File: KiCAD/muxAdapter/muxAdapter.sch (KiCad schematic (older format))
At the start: 55 parts, among them P1 CONN_01X01, P10 CONN_01X01, P11 CONN_01X01, P12 CONN_01X01, P13 CONN_01X01, P14 CONN_01X01, P15 CONN_01X01, P16 CONN_01X01, P17 CONN_01X01, P18 CONN_01X01, P19 CONN_01X01, P2 CONN_01X01, P20 CONN_01X01, P21 CONN_01X01, P22 CONN_01X01, P23 CONN_01X01, P24 CONN_01X01, P25 CONN_01X01, P26 CONN_01X01, P27 CONN_01X01, P28 CONN_01X01, P29 CONN_01X01, P3 CONN_01X01, P30 CONN_01X01, P31 CONN_01X01, P32 CONN_01X01, P33 CONN_01X01, P34 CONN_01X01, P35 CONN_01X01, P36 CONN_01X01, P37 CONN_01X01, P38 CONN_01X01, P39 CONN_01X02, P4 CONN_01X01, P40 CONN_01X02, P41 CONN_01X02, P42 CONN_01X02, P43 CONN_01X02, P44 CONN_01X02, P45 CONN_01X02, P46 CONN_01X02, P5 CONN_01X01, P6 CONN_01X01, P7 CONN_01X01, P8 CONN_01X01, P9 CONN_01X01, U1 MAX14662, U2 MAX14662, U3 PCF8574

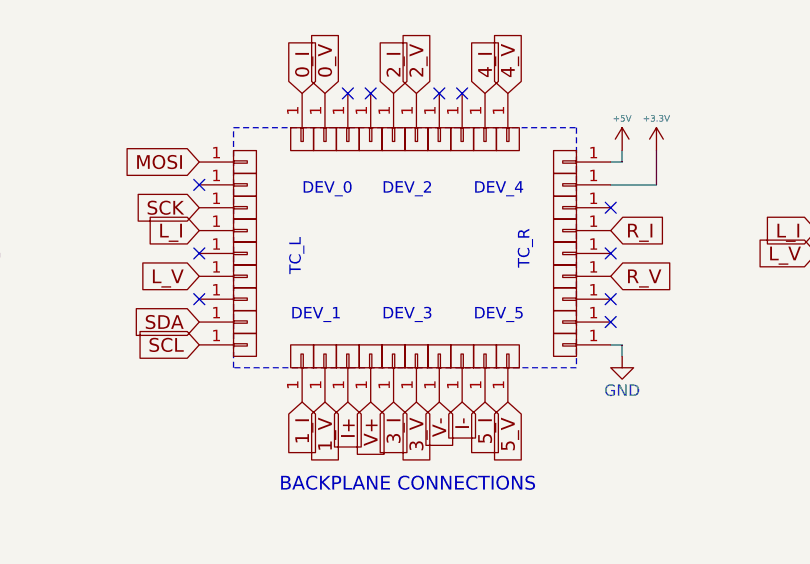
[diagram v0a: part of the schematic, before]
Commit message: order placed for 28x28 mux boards without blind vias
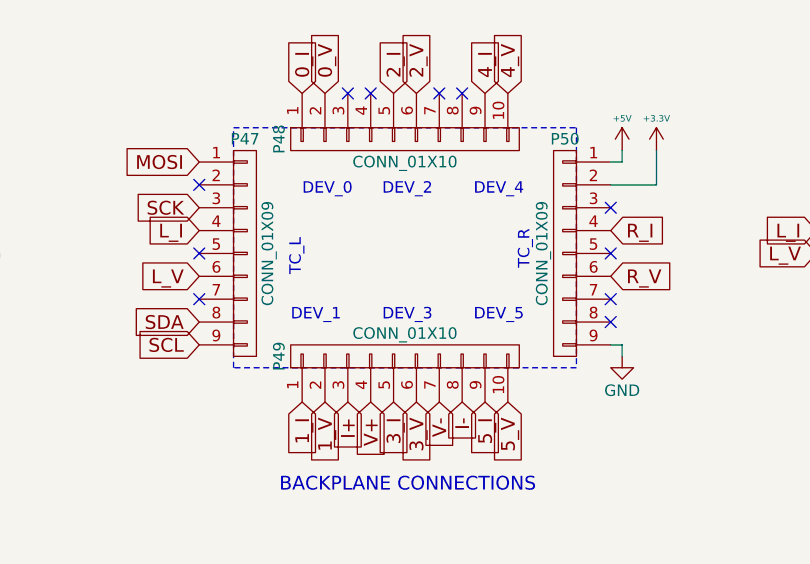
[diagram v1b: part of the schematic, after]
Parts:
- removed P1, P10, P11, P12, P13, P14, P15, P16, P17, P18, P19, P2, P20, P21, P22, P23, P24, P25, P26, P27, P28, P29, P3, P30, P31, P32, P33, P34, P35, P36, P37, P38, P4, P5, P6, P7, P8, P9: CONN_01X01, myparts:0508-0-00-15-00-00-03-0, symbol CONN_01X01
- added P47, P50: CONN_01X09, myparts:TSM-109-01-T-SV, symbol CONN_01X09
- added P48: CONN_01X10, myparts:TSM-110-01-T-SV, symbol CONN_01X10
- added P49: CONN_01X10, myparts:TSM-110-01-T-SV-INV, symbol CONN_01X10
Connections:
- net +3V3: now also P50.2 (P2)
- net +5V: now also P50.1 (P1)
- net 0_I: now also P48.1 (P1)
- net 0_V: now also P48.2 (P2)
- net 1_I: now also P49.1 (P1)
- net 1_V: now also P49.2 (P2)
- net 2_I: now also P48.5 (P5)
- net 2_V: now also P48.6 (P6)
- net 3_I: now also P49.5 (P5)
- net 3_V: now also P49.6 (P6)
- net 4_I: now also P48.9 (P9)
- net 4_V: now also P48.10 (P10)
- net 5_I: now also P49.9 (P9)
- net 5_V: now also P49.10 (P10)
- net GND: now also P50.9 (P9)
- net I+: now also P49.3 (P3)
- net I-: now also P49.8 (P8)
- net L_I: now also P47.4 (P4)
- net L_V: now also P47.6 (P6)
- net MOSI: now also P47.1 (P1)
- net R_I: now also P50.4 (P4)
- net R_V: now also P50.6 (P6)
- net SCK: now also P47.3 (P3)
- net SCL: now also P47.9 (P9)
- net SDA: now also P47.8 (P8)
- net V+: now also P49.4 (P4)
- net V-: now also P49.7 (P7)

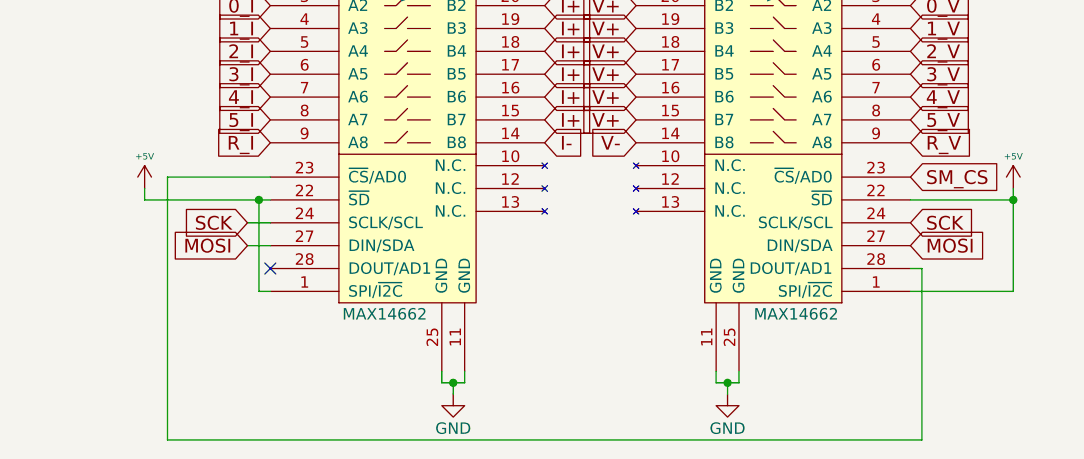
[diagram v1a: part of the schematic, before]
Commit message: fix up some hardware bugs
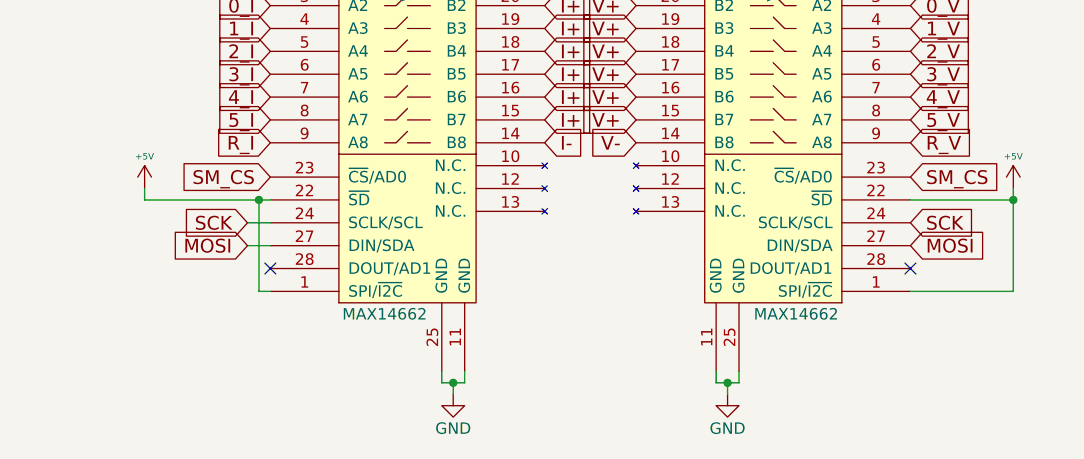
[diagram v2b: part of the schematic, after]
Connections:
- net SM_CS: now also U1.23 (~CS~/AD0)
- net at U2.28 (DOUT/AD1): no longer U1.23 (~CS~/AD0)
- no-connect marks 20 -> 21
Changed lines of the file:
@@
 	5100 5500 5100 5450
-Wire Wire Line
-	5900 4950 5950 4950
-Wire Wire Line
-	5950 4950 5950 5700
-Wire Wire Line
-	5950 5700 2650 5700
-Wire Wire Line
-	2650 5700 2650 4550
-Wire Wire Line
-	2650 4550 3100 4550
 Wire Wire Line
 	3000 4750 3100 4750
@@
 	1    0    0    -1
 $EndComp
+NoConn ~ 5900 4950
+Text GLabel 3100 4550 0    60   Input ~ 0
+SM_CS
 $EndSCHEMATC

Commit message: fix 28x28 adapter chip width
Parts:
- U3: footprint SMD_Packages:SO-16-N -> SMD_Packages:SO-16-W
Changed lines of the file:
@@
 LIBS:valves
 LIBS:muxAdapter-cache
-EELAYER 25 0
+EELAYER 26 0
 EELAYER END
 $Descr A4 11693 8268
@@
 F 0 "U3" H 7350 5000 50  0000 L CNN
 F 1 "PCF8574" H 7800 5000 50  0000 L CNN
-F 2 "SMD_Packages:SO-16-N" H 7700 4400 50  0001 C CNN
+F 2 "SMD_Packages:SO-16-W" H 7700 4400 50  0001 C CNN
 F 3 "" H 7700 4400 50  0000 C CNN
 	1    7700 4400
